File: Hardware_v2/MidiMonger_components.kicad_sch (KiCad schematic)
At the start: 58 parts, among them J1 Conn_01x09_Male, J2 Conn_01x08_Male, J3 Conn_01x08_Male, J4 Conn_01x08_Male, J5 SWD_Header, J6 Eurorack_10_pin_power, U1 STM32F446RETx, U2 TL074, U3 74HCT244, U4 MAX5134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

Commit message: Updates to PCB layout
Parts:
- removed C17: 22uF, Capacitors_SMD:CP_Elec_5x5.3, symbol Device:C_Polarized_Small
- removed J2: Conn_01x08_Male, Connector_PinHeader_2.54mm:PinHeader_1x08_P2.54mm_Vertical, symbol Connector:Conn_01x08_Pin
- added C17: 10uF, Capacitor_SMD:C_0805_2012Metric, symbol Device:C_Small
- added J2: Conn_01x09_Male, Connector_PinHeader_2.54mm:PinHeader_1x09_P2.54mm_Vertical, symbol Connector:Conn_01x09_Pin
- C16: footprint Capacitors_SMD:CP_Elec_5x5.3 -> Capacitor_SMD:CP_Elec_4x5.8
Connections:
- net VCC is gone; now on net +12V: C12.1, C13.1, C16.1, D2.1 (K), U2.4 (V+), U6.3 (VI), U7.3 (VI)
- net VEE is gone; now on net -12V: D3.2 (A), U2.11 (V-)
- net +12V: no longer D2.2 (A), J6.10 (Pin_10), J6.9 (Pin_9)
- net -12V: now also C17.1; no longer D3.1 (K), J6.1 (Pin_1), J6.2 (Pin_2)
- net CV1_LED_OUT: now also J3.2 (Pin_2); no longer J1.6 (Pin_6)
- net CV1_OUT: now also J4.7 (Pin_7); no longer J1.1 (Pin_1)
- net CV2_LED_OUT: now also J3.3 (Pin_3); no longer J1.7 (Pin_7)
- net CV2_OUT: now also J4.6 (Pin_6); no longer J1.2 (Pin_2)
- net CV3_LED_OUT: now also J3.4 (Pin_4); no longer J1.8 (Pin_8)
- net CV3_OUT: now also J4.5 (Pin_5); no longer J1.4 (Pin_4)
- net CV4_LED_OUT: now also J3.5 (Pin_5); no longer J1.9 (Pin_9)
- net CV4_OUT: now also J4.8 (Pin_8); no longer J1.5 (Pin_5)
- net GATE1: now also U1.26 (PB0); no longer U1.23 (PA7)
- net GATE1_LED_OUT: now also J2.1 (Pin_1)
- net GATE1_OUT: now also J1.1 (Pin_1)
- net GATE2: now also U1.24 (PC4); no longer U1.17 (PA3)
- net GATE2_LED_OUT: now also J1.2 (Pin_2)
- net GATE2_OUT: now also J2.2 (Pin_2)
- net GATE3: now also U1.28 (PB2); no longer U1.21 (PA5)
- net GATE3_LED_OUT: now also J2.3 (Pin_3)
- net GATE3_OUT: now also J1.3 (Pin_3)
- net GATE4: now also U1.23 (PA7); no longer U1.25 (PC5)
- net GATE4_LED_OUT: now also J1.4 (Pin_4)
- net GATE4_OUT: now also J2.4 (Pin_4)
- net GATE5: now also U1.33 (PB12); no longer U1.9 (PC1)
- net GATE5_LED_OUT: now also J2.6 (Pin_6); no longer J3.2 (Pin_2)
- net GATE5_OUT: now also J1.6 (Pin_6); no longer J3.4 (Pin_4)
- net GATE6: now also U1.21 (PA5); no longer U1.28 (PB2)
- net GATE6_LED_OUT: now also J1.7 (Pin_7); no longer J4.2 (Pin_2)
- net GATE6_OUT: now also J2.7 (Pin_7); no longer J4.4 (Pin_4)
- net GATE7: now also U1.35 (PB14); no longer U1.40 (PC9)
- net GATE7_LED_OUT: now also J2.9 (Pin_9); no longer J4.1 (Pin_1)
- net GATE7_OUT: now also J1.8 (Pin_8); no longer J3.5 (Pin_5)
- net GATE8: now also U1.17 (PA3); no longer U1.38 (PC7)
- net GATE8_LED_OUT: now also J1.9 (Pin_9); no longer J4.3 (Pin_3)
- net GATE8_OUT: now also J2.8 (Pin_8); no longer J4.5 (Pin_5)
- net GND: now also J1.5 (Pin_5), J4.4 (Pin_4), C17.2, J2.5 (Pin_5); no longer J1.3 (Pin_3), J3.3 (Pin_3), J4.6 (Pin_6)
- net MIDI_DATA: now also J3.7 (Pin_7); no longer J4.7 (Pin_7)
- net MIDI_VREF: now also J3.6 (Pin_6); no longer J4.8 (Pin_8)
- net USB_DM: now also J4.2 (Pin_2); no longer J3.7 (Pin_7)
- net USB_DP: now also J4.3 (Pin_3); no longer J3.6 (Pin_6)
- net USB_VBUS: now also J4.1 (Pin_1); no longer J3.8 (Pin_8)
- new net +12V_IN: D2.2 (A), J6.10 (Pin_10), J6.9 (Pin_9)
- new net -12V_IN: D3.1 (K), J6.1 (Pin_1), J6.2 (Pin_2)
- no-connect marks 29 -> 25
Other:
- moved on the sheet: J3, R1, R2, R3, R4

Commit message: Started Control layout
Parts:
- removed C18: 10uF, Capacitor_SMD:C_0805_2012Metric, symbol Device:C_Small
- added C19: 1uF, Capacitor_SMD:C_0603_1608Metric, symbol Device:C_Small
- added R23: 10k, Resistor_SMD:R_0603_1608Metric, symbol Device:R_Small
- added TP1, TP2, TP3, TP4, TP5, TP6: TestPoint, Custom_Footprints:1mm_Test_Point, symbol Connector:TestPoint
- C17: value 10uF -> 1uF; footprint Capacitor_SMD:C_0805_2012Metric -> Capacitor_SMD:C_0603_1608Metric
- D1: footprint Diodes_SMD:D_SOD-123 -> Diode_SMD:D_SOD-123
- J3, J4: footprint Connector_PinHeader_2.54mm:PinHeader_1x08_P2.54mm_Vertical -> Connector_PinHeader_2.54mm:PinHeader_1x10_P2.54mm_Vertical; symbol Connector:Conn_01x08_Pin -> Connector:Conn_01x10_Pin
- U5: footprint Housings_DIP:DIP-8_W8.89mm_SMDSocket_LongPads -> Package_DIP:DIP-8_W8.89mm_SMDSocket_LongPads
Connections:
- net +12V: now also C19.1, TP1.1
- net +3V3: now also TP3.1
- net +5V: now also J3.9 (Pin_9), TP4.1
- net -12V: now also TP2.1
- net GND: now also J3.8 (Pin_8), C19.2, TP5.1, TP6.1
- net MODE_SWITCH: now also J4.9 (Pin_9)
- net USB_VBUS: now also R23.1; no longer U1.42 (PA9)
- new net: R23.2, U1.42 (PA9)

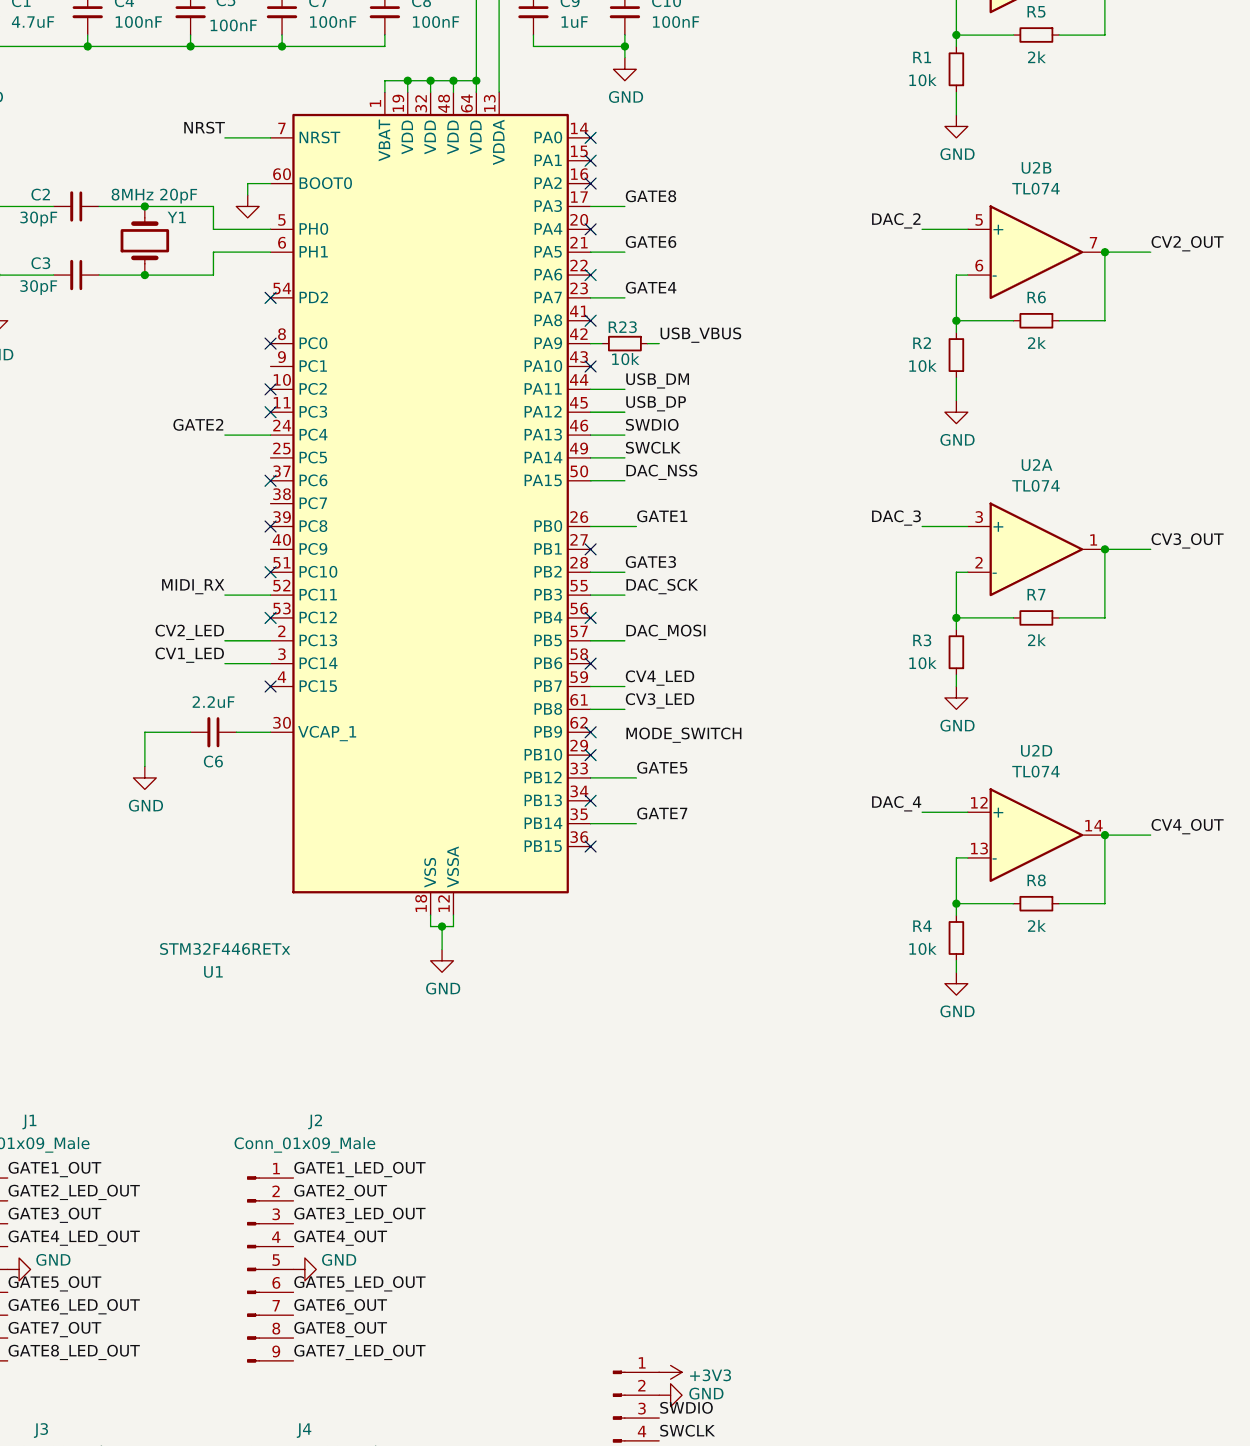
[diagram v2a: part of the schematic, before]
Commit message: Laying out panel
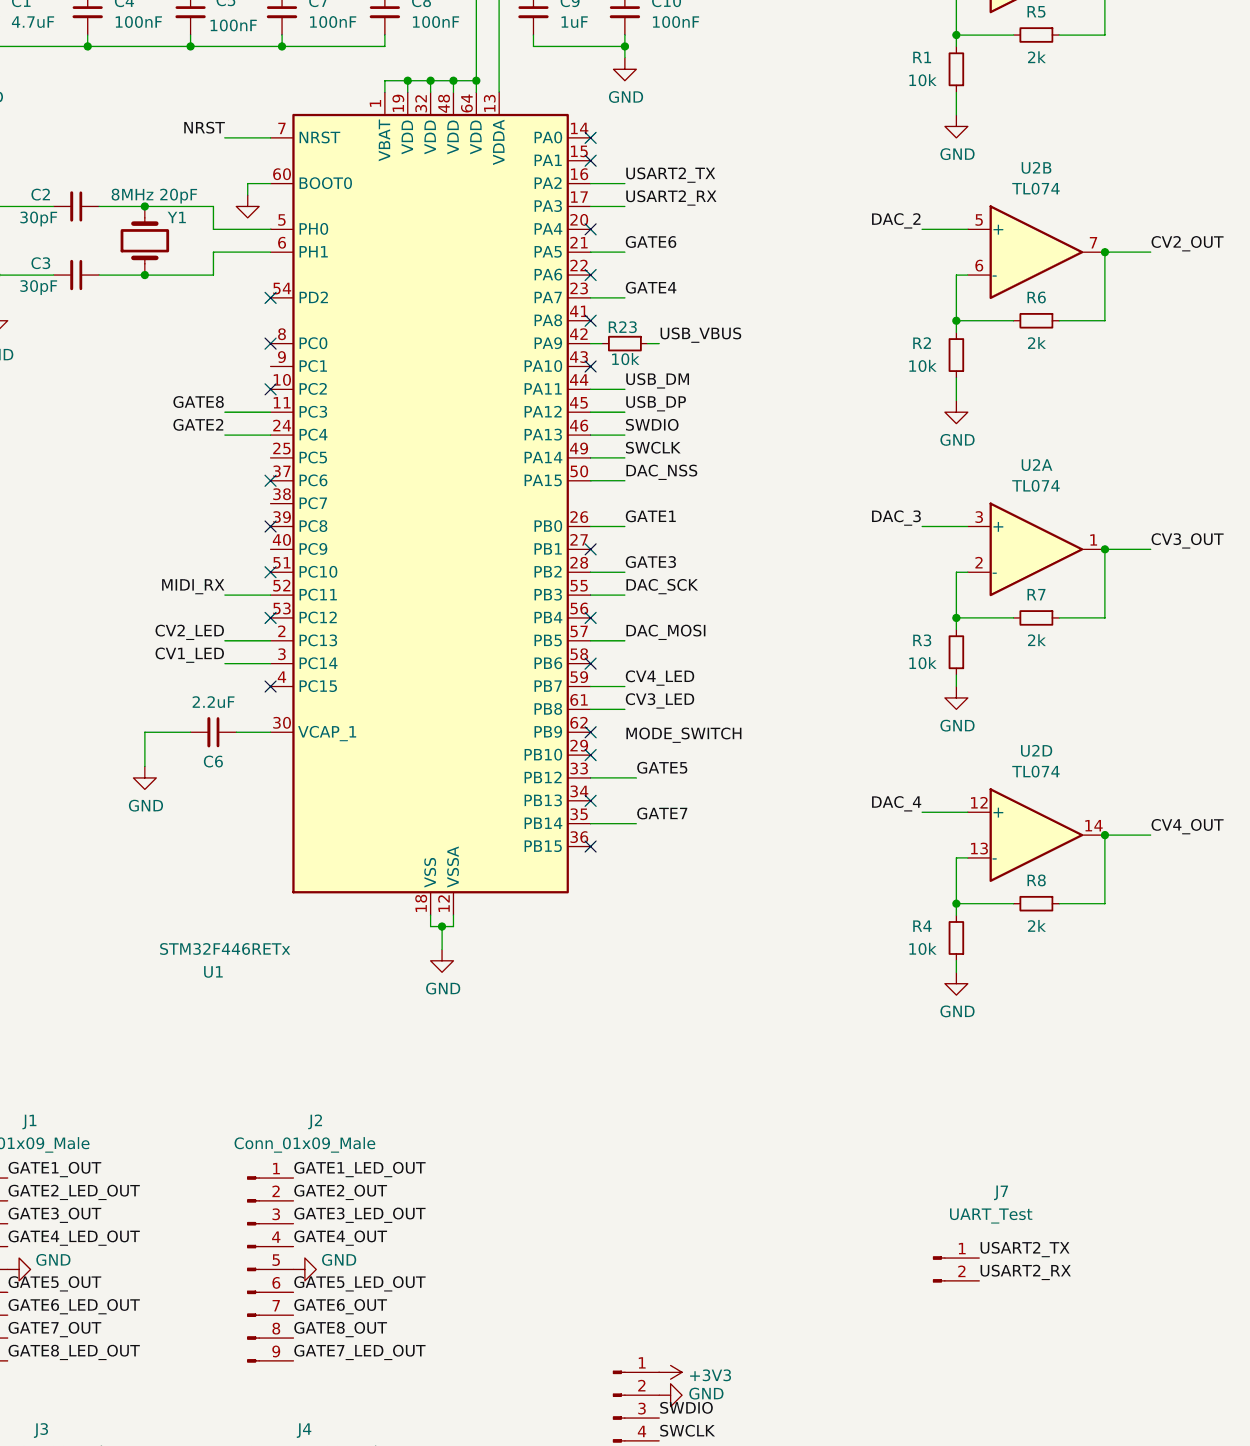
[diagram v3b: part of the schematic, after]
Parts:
- added J7: UART_Test, Connector_PinHeader_2.54mm:PinHeader_1x02_P2.54mm_Vertical, symbol Connector:Conn_01x02_Pin
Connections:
- net GATE8: now also U1.11 (PC3); no longer U1.17 (PA3)
- net USART2_TX: now reaches U1.16 (PA2)
- net USART2_TX: now also J7.1 (Pin_1)
- new net USART2_RX: J7.2 (Pin_2), U1.17 (PA3)
- no-connect marks 25 -> 23
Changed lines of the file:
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@@
 	)
 	(no_connect
-		(at 90.17 52.07)
-	)
-	(no_connect
 		(at 90.17 92.71)
 	)
@@
 	)
 	(no_connect
-		(at 54.61 77.47)
-	)
-	(no_connect
 		(at 90.17 120.65)
 	)
@@
 	(wire
 		(pts
+			(xy 90.17 52.07) (xy 93.98 52.07)
+		)
+		(stroke
+			(width 0)
+			(type default)
+		)
+	)
+	(wire
+		(pts
 			(xy 195.58 91.44) (xy 198.12 91.44)
 		)
@@
 	(wire
 		(pts
-			(xy 90.17 90.17) (xy 95.25 90.17)
+			(xy 90.17 90.17) (xy 93.98 90.17)
 		)
 		(stroke
@@
 	(wire
 		(pts
+			(xy 90.17 54.61) (xy 93.98 54.61)
+		)
+		(stroke
+			(width 0)
+			(type default)
+		)
+	)
+	(wire
+		(pts
 			(xy 90.17 59.69) (xy 93.98 59.69)
 		)
@@
 	(wire
 		(pts
-			(xy 90.17 54.61) (xy 93.98 54.61)
+			(xy 54.61 77.47) (xy 49.53 77.47)
 		)
 		(stroke
@@
 		)
 	)
+	(label "USART2_RX"
+		(at 133.35 173.99 0)
+		(fields_autoplaced yes)
+		(effects
+			(font
+				(size 1.27 1.27)
+			)
+			(justify left bottom)
+		)
+	)
 	(label "GATE8_OUT"
 		(at 57.15 180.34 0)
@@
 		)
 	)
+	(label "USART2_TX"
+		(at 93.98 52.07 0)
+		(fields_autoplaced yes)
+		(effects
+			(font
+				(size 1.27 1.27)
+			)
+			(justify left bottom)
+		)
+	)
 	(label "GATE1"
 		(at 193.04 29.21 180)
@@
 	)
 	(label "GATE8"
-		(at 93.98 54.61 0)
+		(at 49.53 77.47 180)
 		(fields_autoplaced yes)
 		(effects
@@
 				(size 1.27 1.27)
 			)
-			(justify left bottom)
+			(justify right bottom)
 		)
 	)
@@
 		)
 	)
+	(label "USART2_TX"
+		(at 133.35 171.45 0)
+		(fields_autoplaced yes)
+		(effects
+			(font
+				(size 1.27 1.27)
+			)
+			(justify left bottom)
+		)
+	)
 	(label "GATE5"
 		(at 215.9 156.21 180)
@@
 		)
 	)
+	(label "USART2_RX"
+		(at 93.98 54.61 0)
+		(fields_autoplaced yes)
+		(effects
+			(font
+				(size 1.27 1.27)
+			)
+			(justify left bottom)
+		)
+	)
 	(label "CV4_LED"
 		(at 93.98 107.95 0)
@@
 	)
 	(label "GATE1"
-		(at 95.25 90.17 0)
+		(at 93.98 90.17 0)
 		(fields_autoplaced yes)
 		(effects
@@
 					(unit 1)
 				)
+			)
+		)
+	)
+	(symbol
+		(lib_id "Connector:Conn_01x02_Pin")
+		(at 128.27 171.45 0)
+		(unit 1)
+		(exclude_from_sim no)
+		(in_bom yes)
+		(on_board yes)
+		(dnp no)
+		(property "Reference" "J7"
+			(at 135.89 164.084 0)
+			(effects
+				(font
+					(size 1.27 1.27)
+				)
+			)
+		)
+		(property "Value" "UART_Test"
+			(at 134.62 166.624 0)
+			(effects
+				(font
+					(size 1.27 1.27)
+				)
+			)
+		)
+		(property "Footprint" "Connector_PinHeader_2.54mm:PinHeader_1x02_P2.54mm_Vertical"
+			(at 128.27 171.45 0)
+			(effects
+				(font
+					(size 1.27 1.27)
+				)
+				(hide yes)
+			)
+		)
+		(property "Datasheet" "~"
+			(at 128.27 171.45 0)
+			(effects
+				(font
+					(size 1.27 1.27)
+				)
+				(hide yes)
+			)
+		)
+		(property "Description" "Generic connector, single row, 01x02, script generated"
+			(at 128.27 171.45 0)
+			(effects
+				(font
+					(size 1.27 1.27)
+				)
+				(hide yes)
+			)
+		)
+		(pin "1"
+		)
+		(pin "2"
+		)
+		(instances
+			(project "MidiMonger_components"
+				(path "/abb9ca3f-a231-41ea-b48c-42a7557cbf7e"
+					(reference "J7")
+					(unit 1)
+				)

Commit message: Hardware layout
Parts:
- added D4: ESDA6V1BC6, Package_TO_SOT_SMD:SOT-23-6, symbol Power_Protection:ESDA6V1BC6
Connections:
- net GND: now also D4.2 (COM), D4.5 (COM)
- net MODE_SWITCH: now also U1.38 (PC7)
- net USB_DM: now also D4.6 (TVS4)
- net USB_DP: now also D4.3 (TVS2)
- net USB_VBUS: now also D4.4 (TVS3)
- net +12V_IN: no longer names the net of D2.2 (A), J6.10 (Pin_10), J6.9 (Pin_9)
- net -12V_IN: no longer names the net of D3.1 (K), J6.1 (Pin_1), J6.2 (Pin_2)
- no-connect marks 23 -> 29
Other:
- note added: "CV DAC"
- note added: "CV Scaling"
- note added: "Connectors"
- note added: "Gate Scaling"
- note added: "LED resistors"
- note added: "MCU"
- note added: "Power"
- note added: "USB/MIDI protection"
- moved on the sheet: C1, C10, C11, C12, C13, C14, C15, C16, C17, C19, C2, C3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

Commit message: Gerbers prepared for manufacture
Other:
- moved on the sheet: C12, C13, C14, C15, C16, C17, C19, D1, D2, D3, D4, J6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

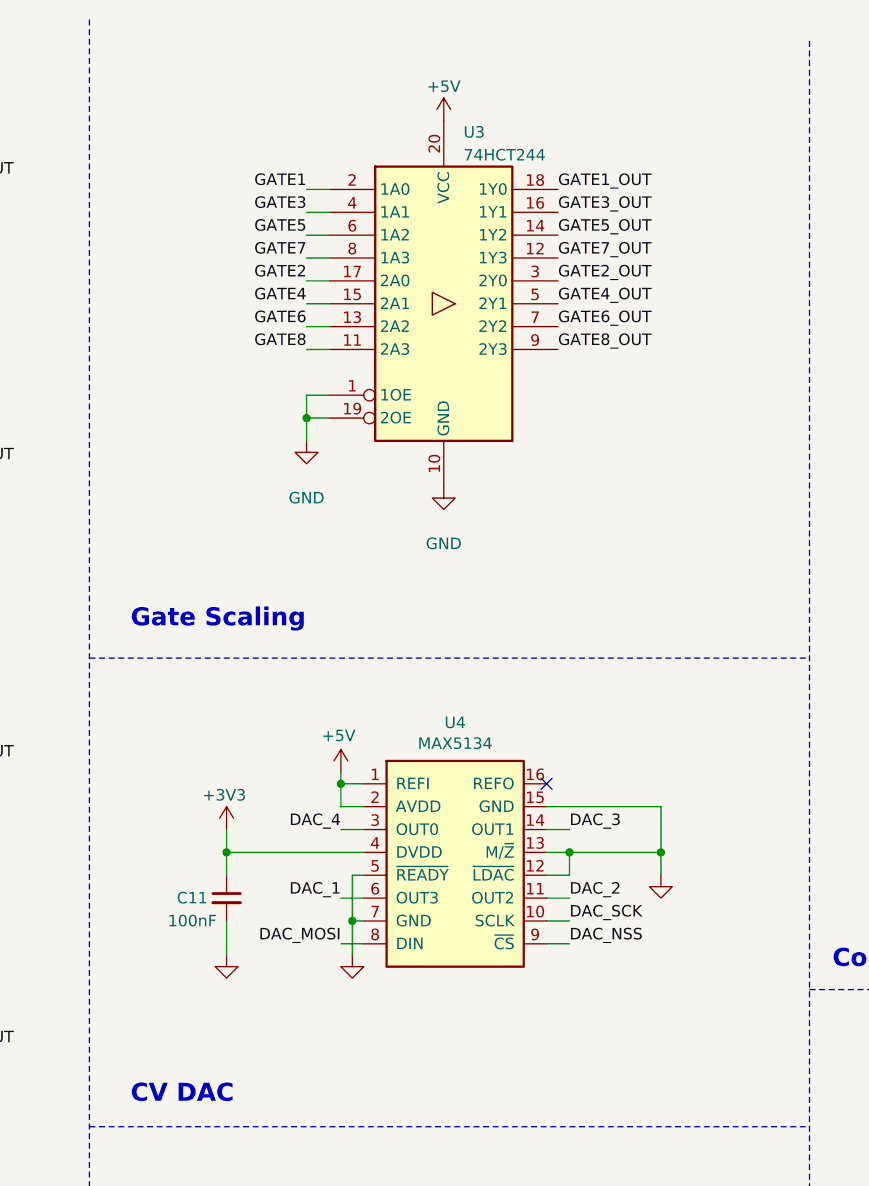
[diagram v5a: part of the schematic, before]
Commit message: Added additional decoupling capacitors to 5V line
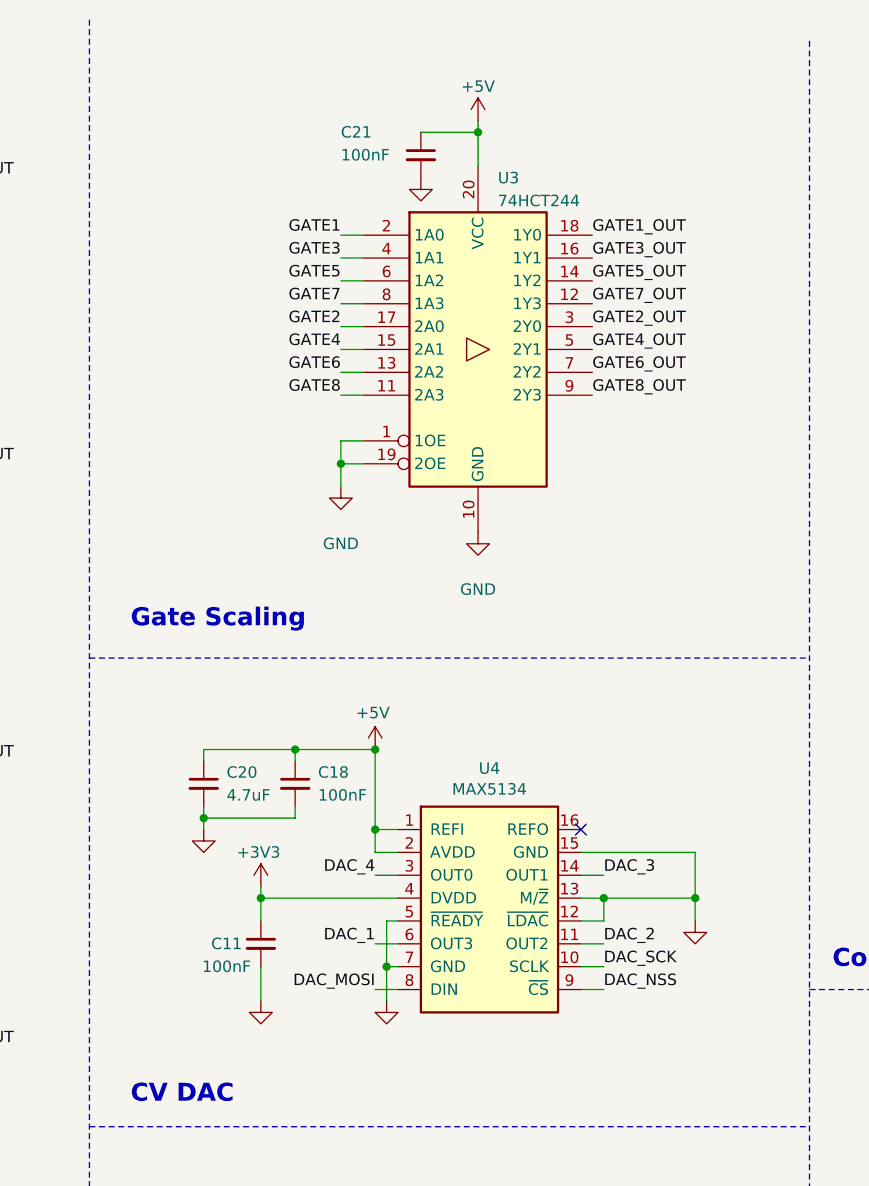
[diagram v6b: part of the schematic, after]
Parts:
- added C18, C21: 100nF, Capacitor_SMD:C_0603_1608Metric, symbol Device:C_Small
- added C20: 4.7uF, Capacitor_SMD:C_0603_1608Metric, symbol Device:C_Small
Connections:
- net +5V: now also C18.1, C20.1, C21.1
- net GND: now also C18.2, C20.2, C21.2
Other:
- moved on the sheet: C11, U3, U4
